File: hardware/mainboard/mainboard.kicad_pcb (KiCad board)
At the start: 4 copper layers, 101 x 30 mm, 48 parts, among them J1 2309407-1, J2 WP7B-S040VA1-R6000, J3 Conn_01x02_Male, J4 AXK7L24223G, J5 503182-1852, J6 WP7B-S040VA1-R6000, U1 TPS65132, U2 MIC5504-1.2YM5-TR, U3 MCP1725-ADJE_MC, U4 TPS65132, U5 ICM-20602

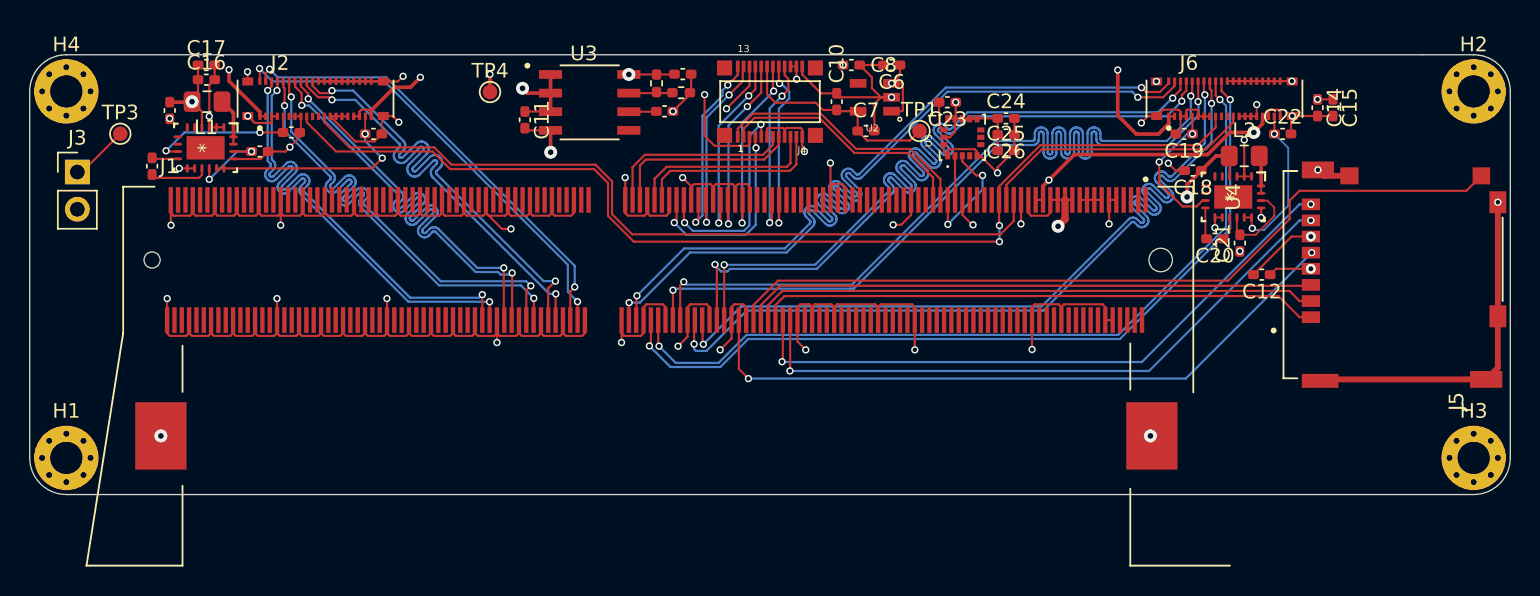
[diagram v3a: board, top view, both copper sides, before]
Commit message: fixed silkscreen
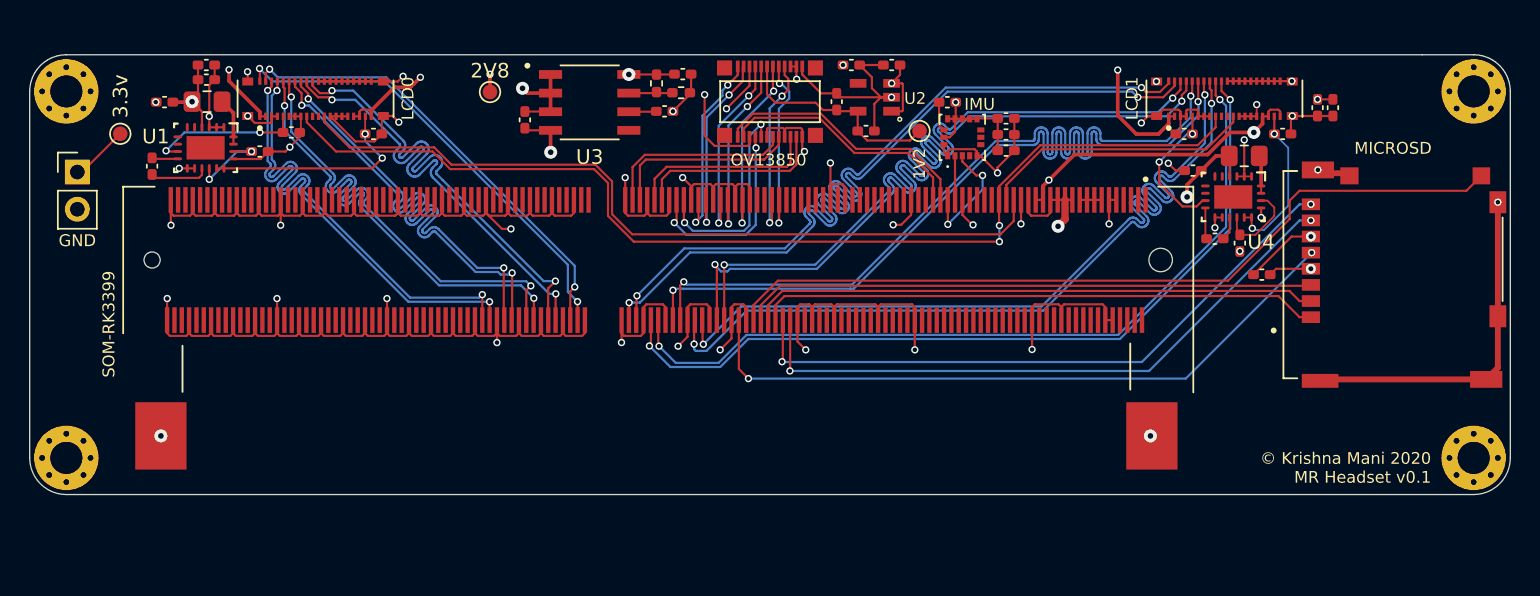
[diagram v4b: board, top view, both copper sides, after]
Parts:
- moved C1 0.67 mm to (98.0, 70.2), turned to 180 degrees
- renumbered TP1 to 1V2, TP4 to 2V8, TP3 to 3.3v
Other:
- board text added: "GND"
- board text added: "IMU"
- board text added: "JLCJLCJLC"
- board text added: "LCD0"
- board text added: "LCD1"
- board text added: "MICROSD"
- board text added: "OV13850"
- board text added: "SOM-RK3399"
- board text added: "© Krishna Mani 2020 MR Headset v0.1"
- board text removed: "© Krishna Mani 2020 MR Headset Mainboard v0.1"

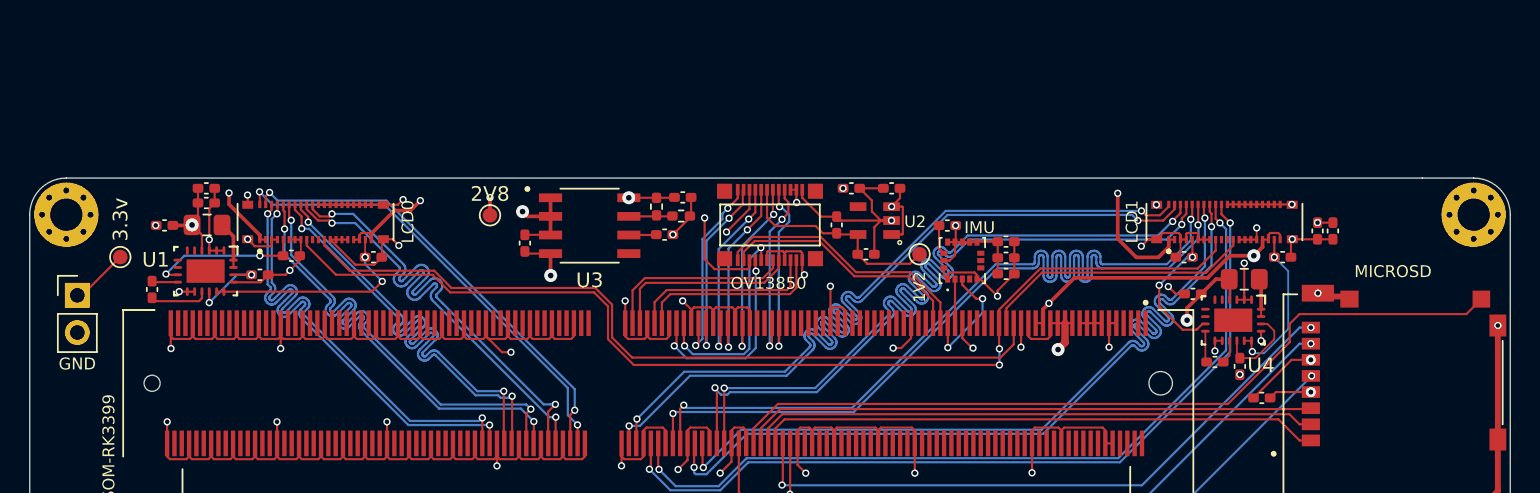
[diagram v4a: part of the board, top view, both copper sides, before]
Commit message: add fpc
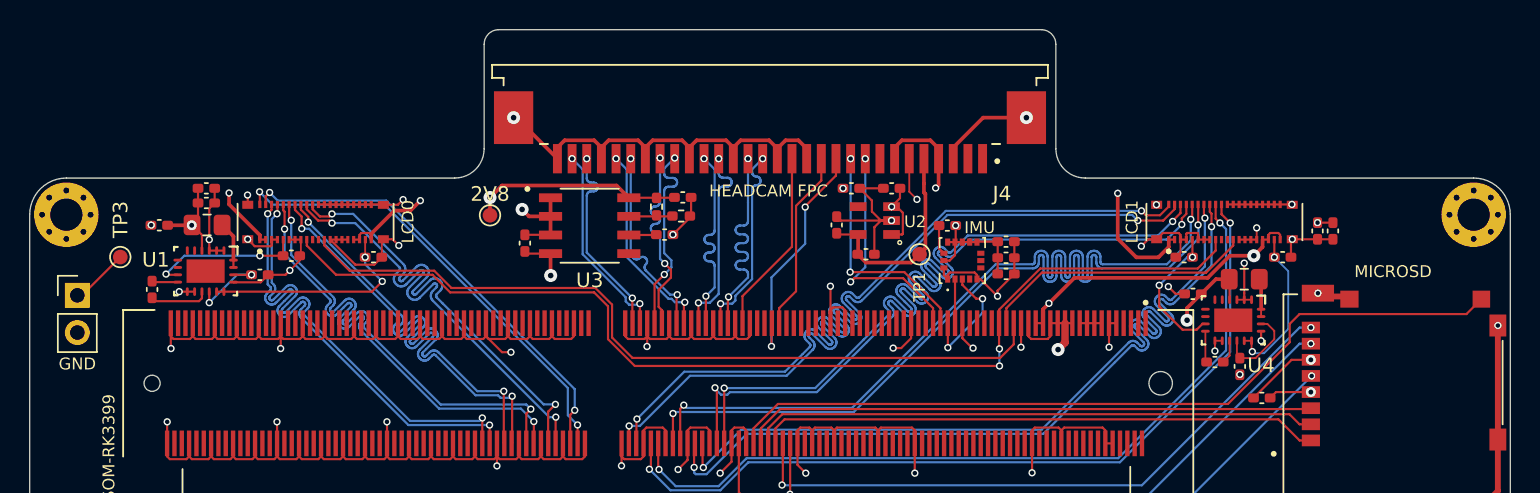
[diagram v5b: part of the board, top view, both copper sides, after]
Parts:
- J4: value AXK7L24223G -> 3-84953-0; footprint mainboard:PANASONIC_AXK7L24223G -> mainboard:TE_3-84953-0
- moved J4 4.52 mm to (139.2, 65.7)
- moved C1 0.36 mm to (97.6, 70.2)
- renumbered 1V2 to TP1, 3.3v to TP3
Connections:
- J4 pad 1: /I2C2_SDA -> (no net)
- J4 pad 10: /MIPI_RX0_D1+ -> /I2C2_SDA
- J4 pad 11: /MIPI_RX0_D1- -> /MIPI_CSI1_RST
- J4 pad 12: GND -> /MIPI_CSI0_PWN
- J4 pad 13: /MIPI_RX0_D2+ -> GND
- J4 pad 14: /MIPI_RX0_D2- -> /GPIO2_B3_CIF_CLKOUTA
- J4 pad 18: +1V2 -> GND
- J4 pad 19: /GPIO2_B3_CIF_CLKOUTA -> /MIPI_RX0_D2+
- J4 pad 2: /I2C2_SCL -> (no net)
- J4 pad 20: /MIPI_CSI0_PWN -> /MIPI_RX0_D2-
- J4 pad 21: /MIPI_CSI1_RST -> GND
- J4 pad 22: +2V8 -> /MIPI_RX0_D1+
- J4 pad 23: +2V8 -> /MIPI_RX0_D1-
- J4 pad 3: +1V8 -> GND
- J4 pad 4: /MIPI_RX0_CLK+ -> +2V8
- J4 pad 5: /MIPI_RX0_CLK- -> +1V2
- J4 pad 6: GND -> +1V8
- J4 pad 7: /MIPI_RX0_D0+ -> +2V8
- J4 pad 8: /MIPI_RX0_D0- -> (no net)
- J4 pad 9: GND -> /I2C2_SCL
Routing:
- net GND: track 312.6 -> 335.9 mm, vias 49 -> 48
- net +2V8: track 80.9 -> 99.5 mm, vias 6 -> 5
- net /MIPI_CSI1_RST: track 12.9 -> 16.2 mm
- net /I2C2_SDA: track 18.1 -> 16.0 mm, vias 0 -> 2
- net /MIPI_RX0_D3-: track 13.3 -> 15.4 mm
- net +1V8: track 108.8 -> 107.4 mm
- net /MIPI_RX0_CLK-: track 14.5 -> 13.7 mm
- net /MIPI_RX0_D0-: track 13.0 -> 13.7 mm, vias 0 -> 2
- net /MIPI_RX0_D1-: track 12.9 -> 13.5 mm, vias 0 -> 2
- net /I2C2_SCL: track 17.0 -> 16.4 mm, vias 0 -> 2
- net /GPIO2_B3_CIF_CLKOUTA: track 13.2 -> 12.6 mm, vias 2 -> 0
- net /MIPI_RX0_D1+: track 13.0 -> 13.5 mm, vias 0 -> 2
- net /MIPI_RX0_D0+: track 13.0 -> 13.5 mm, vias 0 -> 2
- net /MIPI_CSI0_PWN: track 12.9 -> 12.4 mm, vias 2 -> 0
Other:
- board size 101 x 30 mm -> 101 x 40.1 mm
- board text added: "HEADCAM FPC"
- board text removed: "OV13850"

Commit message: bugfixes
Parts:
- removed C12: 100nF, Capacitor_SMD:C_0402_1005Metric_Pad0.74x0.62mm_HandSolder
- added R3: 1k, Resistor_SMD:R_0402_1005Metric_Pad0.72x0.64mm_HandSolder, F.Cu at (140.1, 91.0)
- added R4: 10k, Resistor_SMD:R_0402_1005Metric_Pad0.72x0.64mm_HandSolder, F.Cu at (141.2, 91.0)
- H1, H2, H3, H4: value MountingHole -> MountingHole_Pad
- moved H2 99.2 mm to (91.2, 94.5)
- moved H4 99.2 mm to (187.2, 94.5)
- moved H1 25.0 mm to (91.2, 69.5)
- moved H3 25.0 mm to (187.2, 69.5)
- moved J5 1.50 mm to (181.0, 82.0), turned to 270 degrees
- renumbered 2V8 to TP4
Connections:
- H1 pad 1: (no net) -> GND
- H2 pad 1: (no net) -> GND
- H3 pad 1: (no net) -> GND
- H4 pad 1: (no net) -> GND
- J1 pad 76: (no net) -> +3V3
- J5 pad DT: /SDMMC0_DET_L -> Net-(J5-PadDT)
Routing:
- net /SDMMC0_DET_L: track 55.1 -> 7.37 mm
- net Net-(J5-PadDT): track 0.00 -> 36.7 mm
- net /SDMMC0_D3: track 38.7 -> 55.0 mm, vias 0 -> 2
- net /SDMMC0_D2: track 38.4 -> 54.2 mm, vias 0 -> 2
- net /SDMMC0_CMD: track 39.1 -> 54.9 mm, vias 0 -> 2
- net /SDMMC0_D1: track 43.4 -> 51.9 mm, vias 2 -> 0
- net /SDMMC0_D0: track 43.3 -> 51.1 mm, vias 2 -> 0
- net /SDMMC0_CLK: track 46.3 -> 50.9 mm, vias 2 -> 0
- net GND: track 335.9 -> 334.7 mm
- net +3V3: track 38.4 -> 37.4 mm, vias 7 -> 9
- net /LCD 2/AVDD: track 10.9 -> 10.0 mm
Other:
- board text added: "1V2"
- board text added: "2V8"
- board text added: "3.3v"

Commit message: minor fix
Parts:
- moved R3 1.70 mm to (140.1, 89.3)
- moved R4 1.70 mm to (141.2, 89.3)
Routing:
- net /SDMMC0_DET_L: track 7.37 -> 5.67 mm
- net /SDMMC0_D0: track 51.1 -> 49.9 mm
- net /SDMMC0_D1: track 51.9 -> 50.8 mm
- net Net-(J5-PadDT): track 36.7 -> 35.6 mm

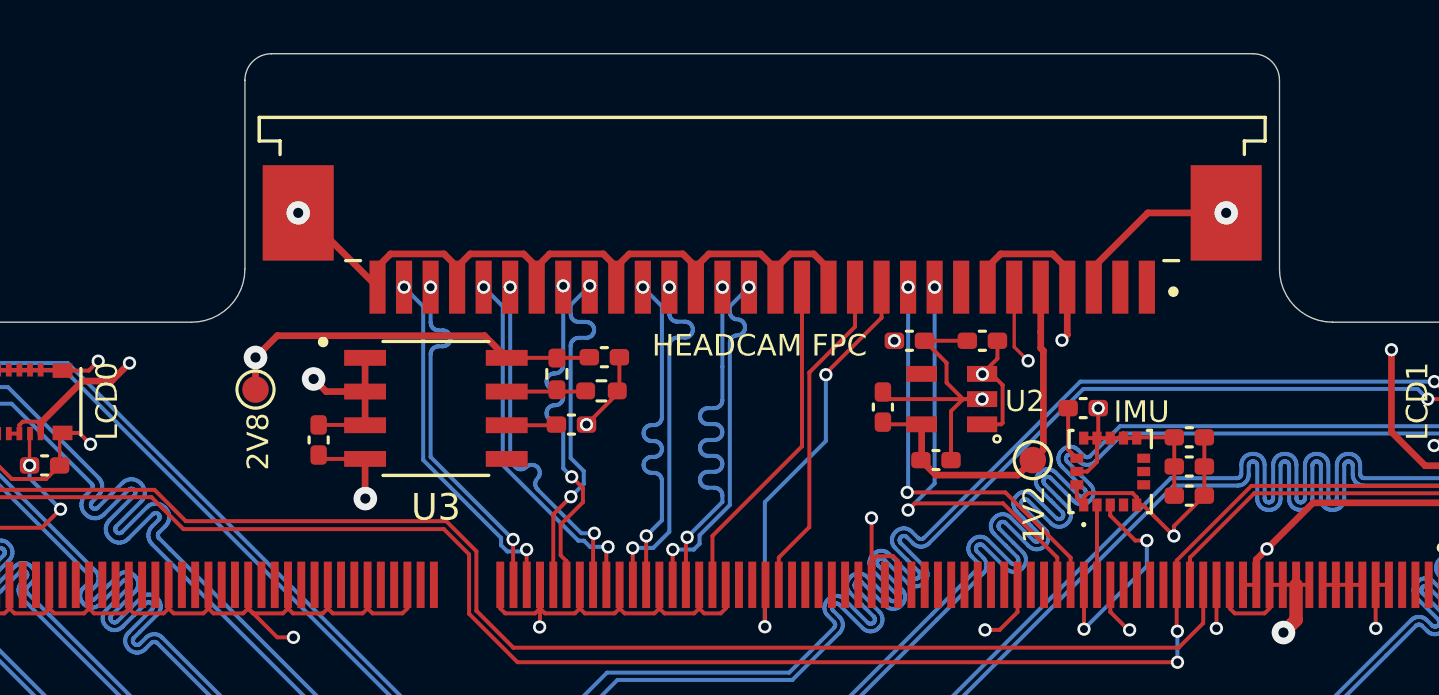
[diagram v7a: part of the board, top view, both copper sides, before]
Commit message: 3d models, 1v2 regulator footprint change
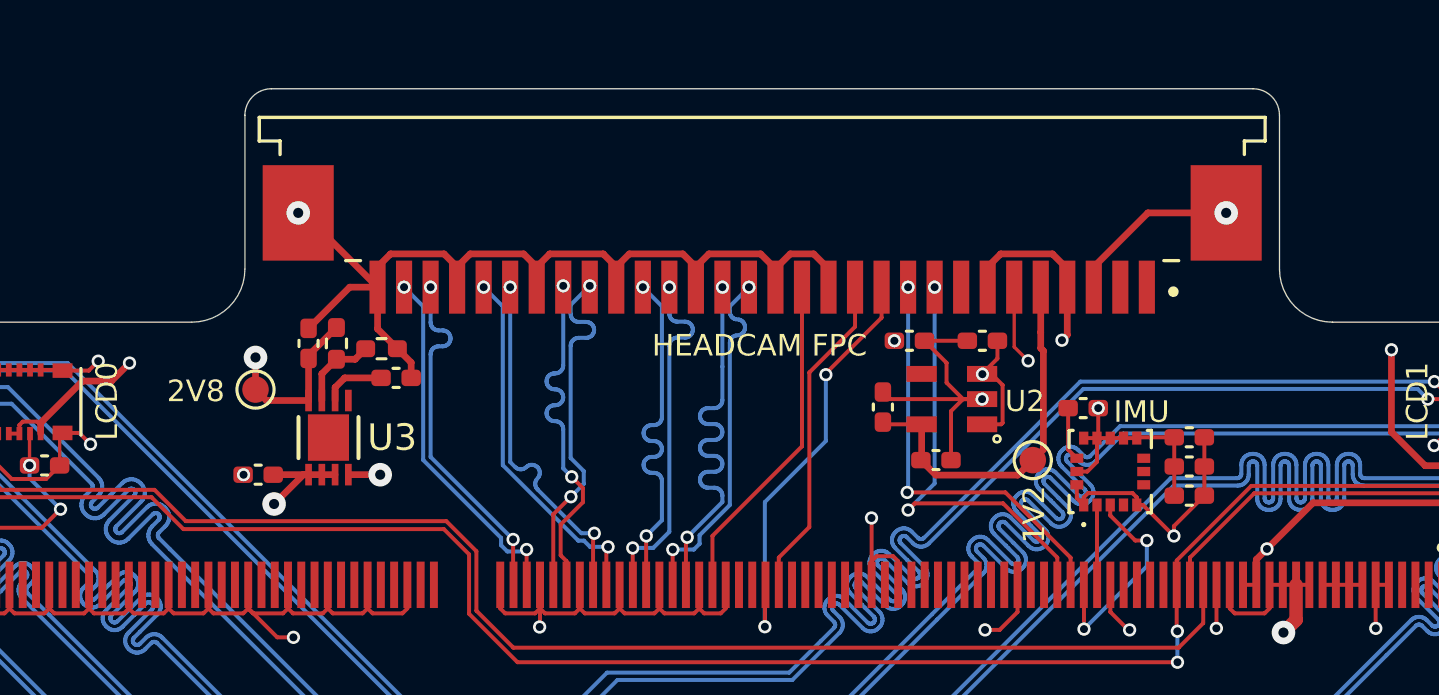
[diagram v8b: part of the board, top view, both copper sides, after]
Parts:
- U3: footprint mainboard:SOIC127P599X175-8N -> mainboard:MCP1725-ADJE_MC
- moved C13 11.2 mm to (122.2, 67.8), turned to 90 degrees
- moved R2 8.44 mm to (124.9, 68.0)
- moved R1 8.39 mm to (123.2, 67.8)
- moved C9 6.84 mm to (125.5, 69.1)
- moved U3 4.20 mm to (122.9, 71.3), turned to 90 degrees
- moved C11 2.63 mm to (120.2, 72.8), turned to 180 degrees
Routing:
- net +2V8: track 99.5 -> 91.6 mm
- net +3V3: track 37.4 -> 35.1 mm
- net GND: track 334.7 -> 336.8 mm
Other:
- board size 101 x 40.1 mm -> 101 x 38.8 mm
